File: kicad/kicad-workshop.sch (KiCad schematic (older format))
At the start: 21 parts, among them J1 TYPE-C-31-M-12, J2 Conn_01x04, J3 Conn_01x04, SW2 PEC12R-4130F-S0012, U1 EFM32HG309F64G-B-QFN24

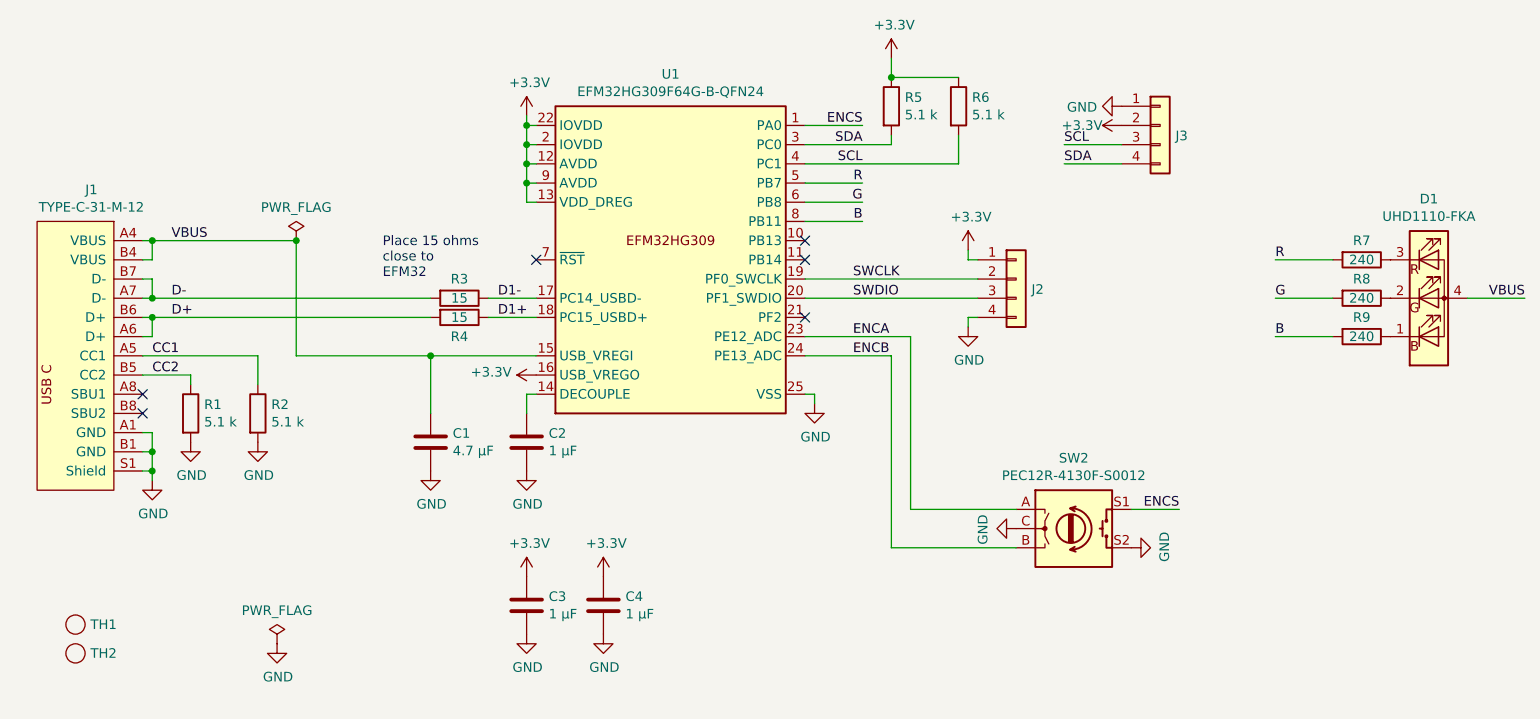
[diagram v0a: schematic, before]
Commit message: change LED to single color The 1x1 mm LED was too difficult for assembly, mostly locating pin 1
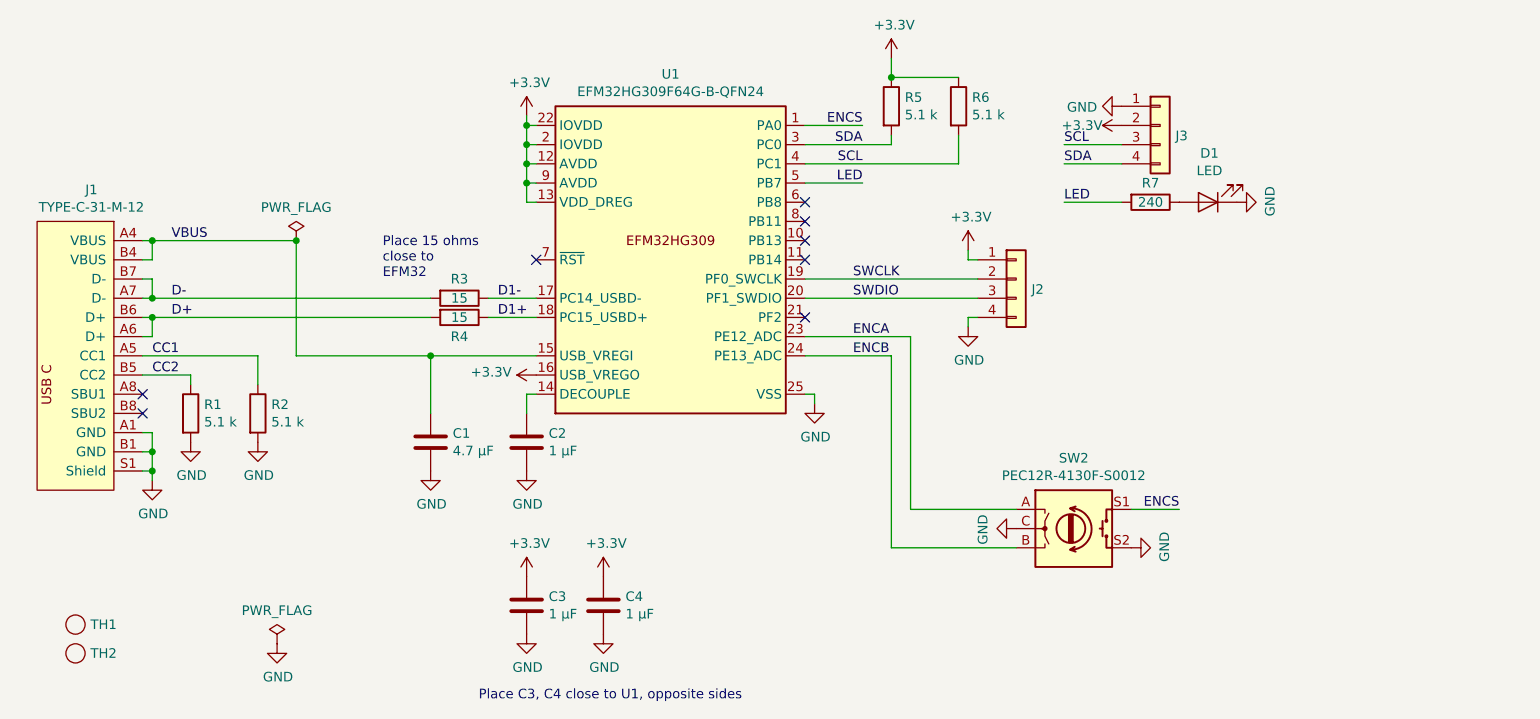
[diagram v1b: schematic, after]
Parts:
- removed D1: UHD1110-FKA, kicad_pcb:LED_cree_4_1x1, symbol kicad-workshop:UHD1110-FKA
- removed R8, R9: 240, kicad-workshop:R_0603_1608Metric, symbol Device:R
- added D1: LED, LED_SMD:LED_0603_1608Metric, symbol Device:LED
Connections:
- net GND: now also D1.1 (K)
- net at R7.1: now also D1.2 (A)
- net B: no longer names the net of U1.8 (PB11)
- net G: no longer names the net of U1.6 (PB8)
- net R renamed LED
- no-connect marks 6 -> 8
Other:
- note added: "Place C3, C4 close to U1, opposite sides"
- moved on the sheet: R7
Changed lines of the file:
@@
 EESchema Schematic File Version 4
-EELAYER 29 0
+LIBS:kicad-workshop-cache
+EELAYER 30 0
 EELAYER END
 $Descr USLetter 11000 8500
@@
 Wire Wire Line
 	4900 3250 5200 3250
-Wire Wire Line
-	4900 3350 5200 3350
-Text Label 5200 3250 2    50   ~ 0
-R
-Text Label 5200 3350 2    50   ~ 0
-G
-Wire Wire Line
-	4900 3450 5200 3450
-Text Label 5200 3450 2    50   ~ 0
-B
 $Comp
 L Device:R R5
@@
 SDA
 $Comp
-L kicad-workshop:UHD1110-FKA D1
-U 1 1 5D33B19C
-P 8150 3850
-F 0 "D1" H 8150 4367 50  0000 C CNN
-F 1 "UHD1110-FKA" H 8150 4276 50  0000 C CNN
-F 2 "kicad_pcb:LED_cree_4_1x1" H 8150 4350 50  0001 C CNN
-F 3 "https://www.cree.com/led-components/media/documents/ds-UHD1110-FKA.pdf" H 8150 3400 50  0001 C CNN
-	1    8150 3850
-	1    0    0    -1
-$EndComp
-$Comp
 L Device:R R7
 U 1 1 5D33ED28
-P 7800 3650
-F 0 "R7" V 7700 3650 50  0000 C CNN
-F 1 "240" V 7800 3650 50  0000 C CNN
-F 2 "kicad-workshop:R_0603_1608Metric" V 7730 3650 50  0001 C CNN
-F 3 "~" H 7800 3650 50  0001 C CNN
-	1    7800 3650
+P 6700 3350
+F 0 "R7" V 6600 3350 50  0000 C CNN
+F 1 "240" V 6700 3350 50  0000 C CNN
+F 2 "kicad-workshop:R_0603_1608Metric" V 6630 3350 50  0001 C CNN
+F 3 "~" H 6700 3350 50  0001 C CNN
+	1    6700 3350
 	0    1    1    0
 $EndComp
-$Comp
-L Device:R R8
-U 1 1 5D33FB01
-P 7800 3850
-F 0 "R8" V 7700 3850 50  0000 C CNN
-F 1 "240" V 7800 3850 50  0000 C CNN
-F 2 "kicad-workshop:R_0603_1608Metric" V 7730 3850 50  0001 C CNN
-F 3 "~" H 7800 3850 50  0001 C CNN
-	1    7800 3850
-	0    1    1    0
-$EndComp
-$Comp
-L Device:R R9
-U 1 1 5D33FE1C
-P 7800 4050
-F 0 "R9" V 7700 4050 50  0000 C CNN
-F 1 "240" V 7800 4050 50  0000 C CNN
-F 2 "kicad-workshop:R_0603_1608Metric" V 7730 4050 50  0001 C CNN
-F 3 "~" H 7800 4050 50  0001 C CNN
-	1    7800 4050
-	0    1    1    0
-$EndComp
-Text Label 8650 3850 2    50   ~ 0
-VBUS
-Wire Wire Line
-	8650 3850 8350 3850
-Wire Wire Line
-	7650 3650 7350 3650
-Wire Wire Line
-	7650 3850 7350 3850
-Text Label 7350 3650 0    50   ~ 0
-R
-Text Label 7350 3850 0    50   ~ 0
-G
-Wire Wire Line
-	7650 4050 7350 4050
-Text Label 7350 4050 0    50   ~ 0
-B
+Wire Wire Line
+	6550 3350 6250 3350
+Text Label 6250 3350 0    50   ~ 0
+LED
 Text Label 5150 3750 0    50   ~ 0
 SWCLK
@@
 	1    0    0    -1
 $EndComp
+$Comp
+L Device:LED D1
+U 1 1 5DBDCDE8
+P 7000 3350
+F 0 "D1" H 6993 3095 50  0000 C CNN
+F 1 "LED" H 6993 3186 50  0000 C CNN
+F 2 "LED_SMD:LED_0603_1608Metric" H 7000 3350 50  0001 C CNN
+F 3 "~" H 7000 3350 50  0001 C CNN
+	1    7000 3350
+	-1   0    0    1
+$EndComp
+$Comp
+L power:GND #PWR0118
+U 1 1 5DBE3751
+P 7150 3350
+F 0 "#PWR0118" H 7150 3100 50  0001 C CNN
+F 1 "GND" H 7155 3177 50  0000 C CNN
+F 2 "" H 7150 3350 50  0001 C CNN
+F 3 "" H 7150 3350 50  0001 C CNN
+	1    7150 3350
+	0    -1   -1   0
+$EndComp
+Text Label 5200 3250 2    50   ~ 0
+LED
+NoConn ~ 4900 3450
+NoConn ~ 4900 3350
+Text Notes 3200 5950 0    50   ~ 0
+Place C3, C4 close to U1, opposite sides
 $EndSCHEMATC
